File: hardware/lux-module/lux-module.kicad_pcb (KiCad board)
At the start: 2 copper layers, 21.6 x 21.6 mm, 9 parts, among them J1 Conn_01x04, U1 TSL25911FN, U2 TPD3E001DRLR

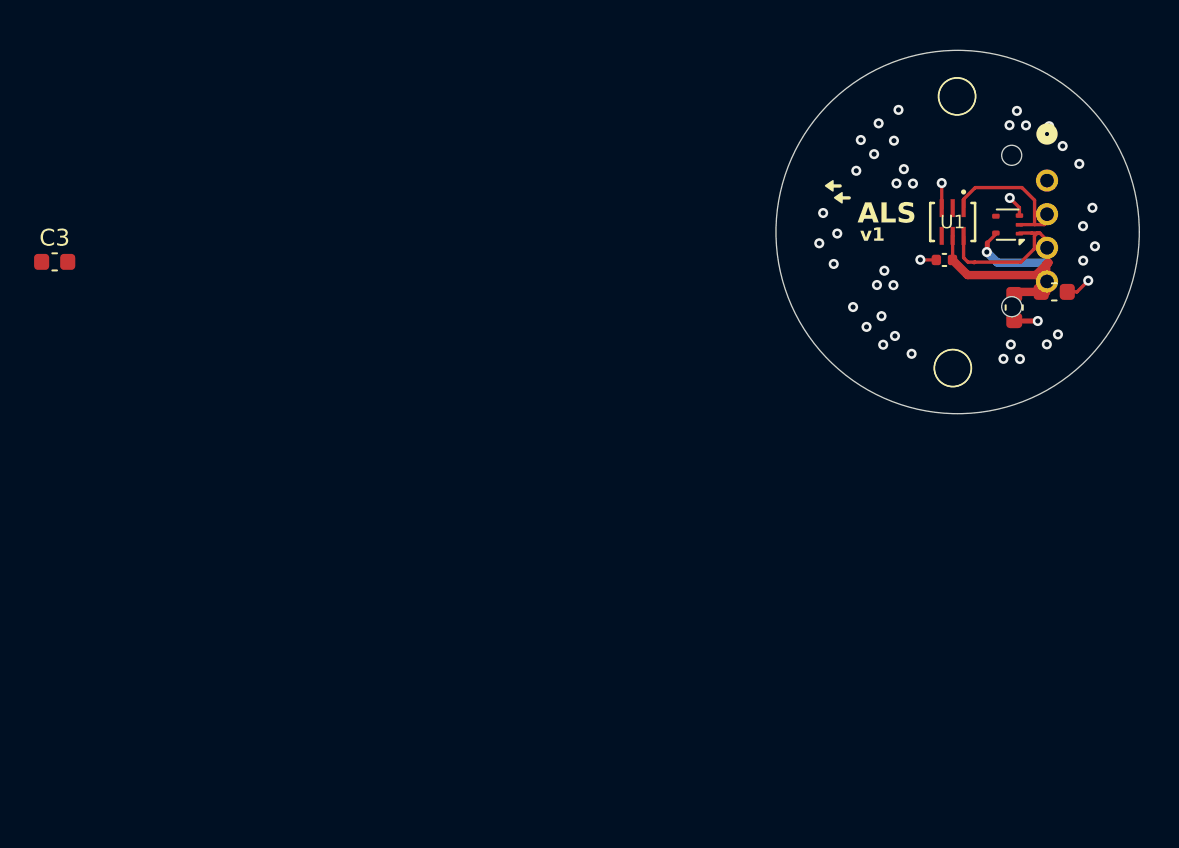
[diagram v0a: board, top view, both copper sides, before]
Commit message: connector fixes
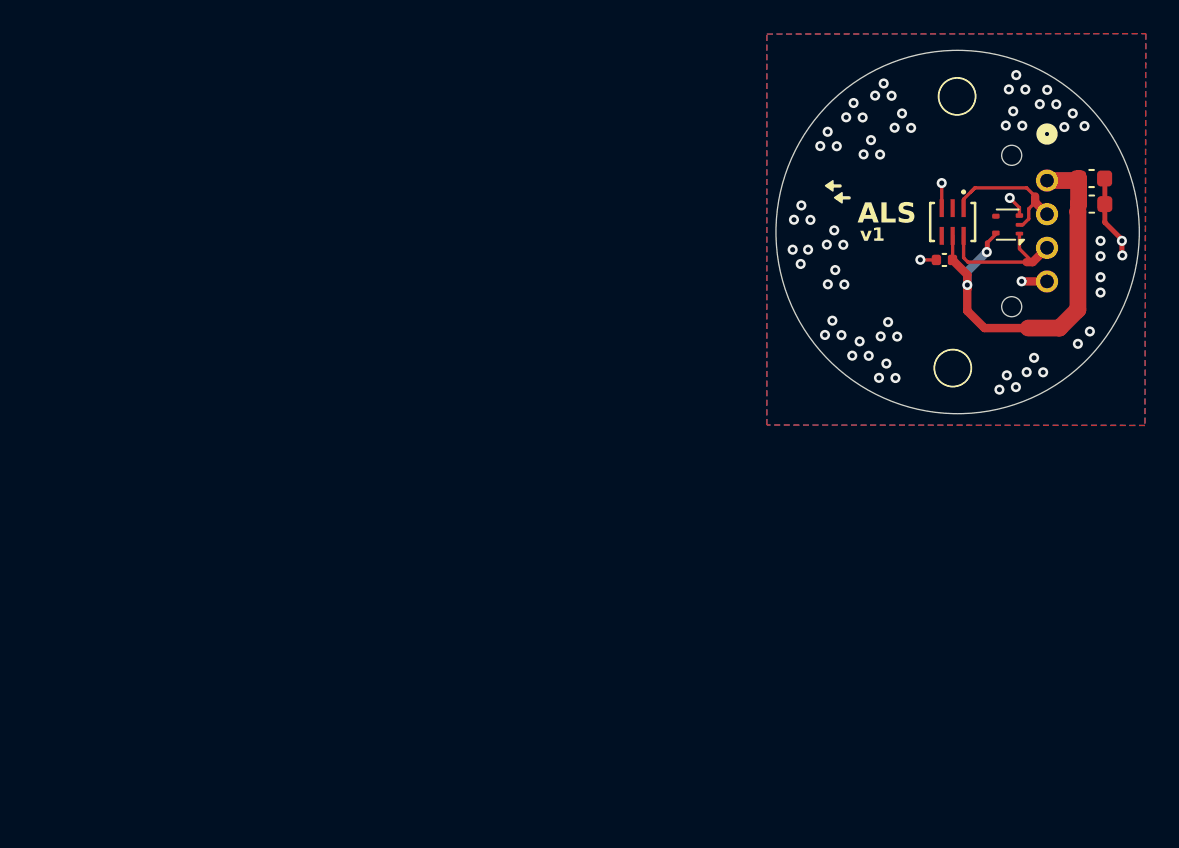
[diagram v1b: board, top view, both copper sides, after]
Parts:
- removed the C3 at (79.6, 55.9)
- moved C3 7.69 mm to (141.2, 52.5), turned to 0 degrees
- moved C2 7.10 mm to (141.2, 50.9)
- renumbered Ce to C3
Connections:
- J1 pad 2: /SDA -> /SCL
- J1 pad 3: /SCL -> /SDA
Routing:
- net +3V3: track 16.9 -> 25.6 mm, vias 1 -> 2
- net GND: track 6.97 -> 10.2 mm, vias 42 -> 69
- added copper zone on B.Cu, net GND
- added copper zone on F.Cu, net GND
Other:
- board text added: "VCC SCL SDA VSS"
- board text removed: "GND"
- board text removed: "SCL"
- board text removed: "SDA"
- board text removed: "VCC"

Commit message: work
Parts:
- C1: footprint Capacitor_SMD:C_0402_1005Metric -> Capacitor_SMD:C_0805_2012Metric
- C2, C3: footprint Capacitor_SMD:C_0603_1608Metric -> Capacitor_SMD:C_0805_2012Metric
- moved C1 1.13 mm to (131.9, 56.8)
- moved C3 0.66 mm to (141.2, 53.1)
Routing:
- net GND: track 10.2 -> 10.1 mm, vias 69 -> 77
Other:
- board text added: "js"
- board text removed: "JS"

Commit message: update ALS
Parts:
- added D1: LED, LED_SMD:LED_0603_1608Metric, F.Cu at (97.7, 84.5)
- added G***: LOGO, LOGO, B.Cu at (104.7, 77.7)
- added H3: MountingHole, MountingHole:MountingHole_2.2mm_M2, F.Cu at (104.2, 72.7)
- added H4: MountingHole, MountingHole:MountingHole_2.2mm_M2, F.Cu at (104.2, 84.4)
- added R1: 470, Resistor_SMD:R_0402_1005Metric, F.Cu at (95.4, 84.3)
- moved H2 57.4 mm to (90.4, 84.3)
- moved C2 57.3 mm to (90.1, 76.8), turned to 180 degrees
- moved C3 57.2 mm to (90.1, 78.8), turned to 180 degrees
- moved J1 49.7 mm to (94.4, 73.9), turned to 0 degrees
- moved U2 44.8 mm to (97.8, 76.6), turned to 0 degrees
- moved U1 44.3 mm to (97.3, 79.8), turned to 0 degrees
- moved H1 43.8 mm to (90.4, 72.7)
- moved C1 38.7 mm to (100.9, 79.9), turned to 0 degrees
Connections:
- U2 pad 1: /SDA -> /SCL
- U2 pad 2: /SCL -> /SDA
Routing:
- net GND: track 10.1 -> 2.72 mm, vias 77 -> 67
- net /SCL: track 8.48 -> 12.1 mm, vias 0 -> 2
- net /SDA: track 8.74 -> 9.86 mm
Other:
- board size 21.6 x 21.6 mm -> 20 x 18 mm
- board text added: "-"
- board text added: "SC"
- board text added: "SD"
- board text added: "VC"
- board text added: "VS"
- board text added: "adr - 0x29"
- board text added: "dev by jeevan"
- board text added: "lux"
- board text added: "module"
- board text added: "on"
- board text added: "v1.0 - 2026"
- board text added: "vc - 3V3"
- board text removed: "2026"
- board text removed: "M2"
- board text removed: "VCC SCL SDA VSS"
- board text removed: "homectrl"
- board text removed: "js"
- board text removed: "|"
